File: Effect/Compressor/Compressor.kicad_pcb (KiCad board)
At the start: 2 copper layers, 30 x 62 mm, 33 parts, among them J1 Conn_01x04_Pin, J2 Conn_01x04_Pin, Q1 MMBF5103, Q2 NMB2227A, Q3 MMBF5103

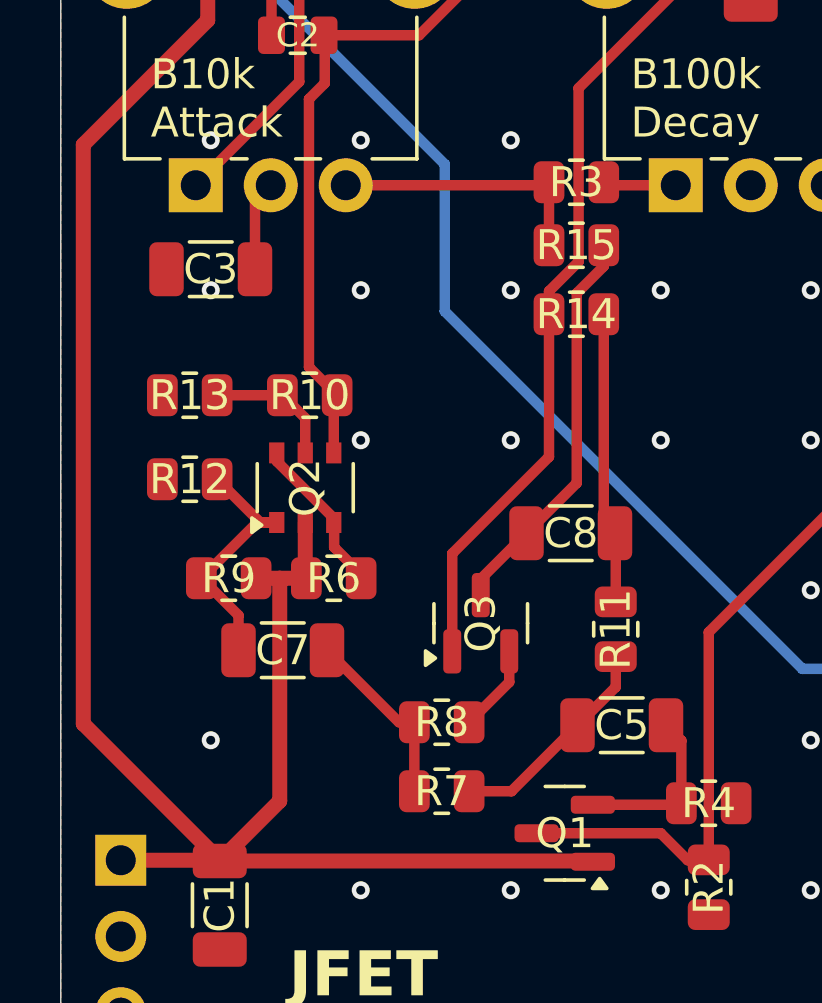
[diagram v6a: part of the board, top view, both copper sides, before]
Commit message: Update some compressor component values based on testing
I think I was being a bit too timid wrt the compressor, making it a bit
boring.  It definitely works, but it looks more interesting with a much
more aggressive compression ratio, and a more aggressive signal
amplification to match.

The level trim pot was also slow to respond because the capacitor to
keep it stable was fairly large.

Also, partially bypass the emitter resistor in the amplification stage
to give higher frequencies a bit more oomph - the AC signal analysis
claims they otherwise attenuated over 10kHz.

Most of this was tested with the old boards (just changed components).
And other parts are "this looks better in simulation" (eg the emitter
resistor bypassing).

Signed-off-by: Linus Torvalds <torvalds@linux-foundation.org>
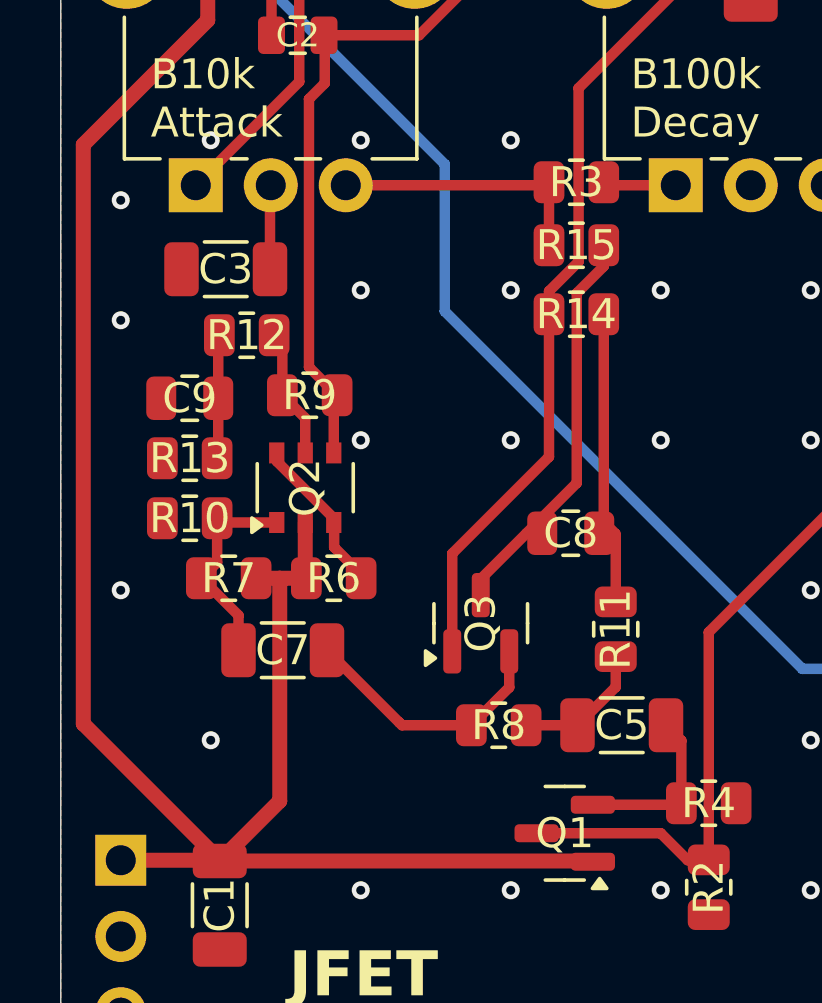
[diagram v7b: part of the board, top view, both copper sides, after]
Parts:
- removed the R8 at (97.7, 109.4)
- added C9: 22nF, Capacitor_SMD:C_0805_2012Metric, F.Cu at (89.3, 98.6)
- added R12: 470, Resistor_SMD:R_0805_2012Metric, F.Cu at (91.2, 96.5)
- C3: value 0.47uF -> 1uF
- C4: value 22uF -> 10uF
- C8: footprint Capacitor_SMD:C_1206_3216Metric -> Capacitor_SMD:C_0805_2012Metric
- R13: value 1k -> 470
- R8: renamed from R7; value 1k -> 470
- R9: renamed from R10; value 2k2 -> 10k
- moved R8 2.91 mm to (99.6, 109.5)
- moved R13 2.10 mm to (89.3, 100.6)
- moved R10 1.30 mm to (89.3, 102.6)
- moved C3 0.50 mm to (90.5, 94.3)
- renumbered R12 to R10, R9 to R7
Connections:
- Q3 pad 2: Net-(Q3-S) -> AMP_IN
- R13 pad 1: Net-(Q2A-E1) -> Net-(C9-Pad2)
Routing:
- net Net-(C9-Pad2): track 0.00 -> 4.13 mm
- net Net-(Q3-S): track 2.92 -> 0.00 mm
- net Net-(C5-Pad2): track 7.34 -> 4.53 mm
- net AMP_IN: track 6.21 -> 8.83 mm
- net Net-(Q2A-B1): track 8.78 -> 7.18 mm
- net Net-(Q3-G): track 14.1 -> 13.4 mm
- net GND: vias 39 -> 41

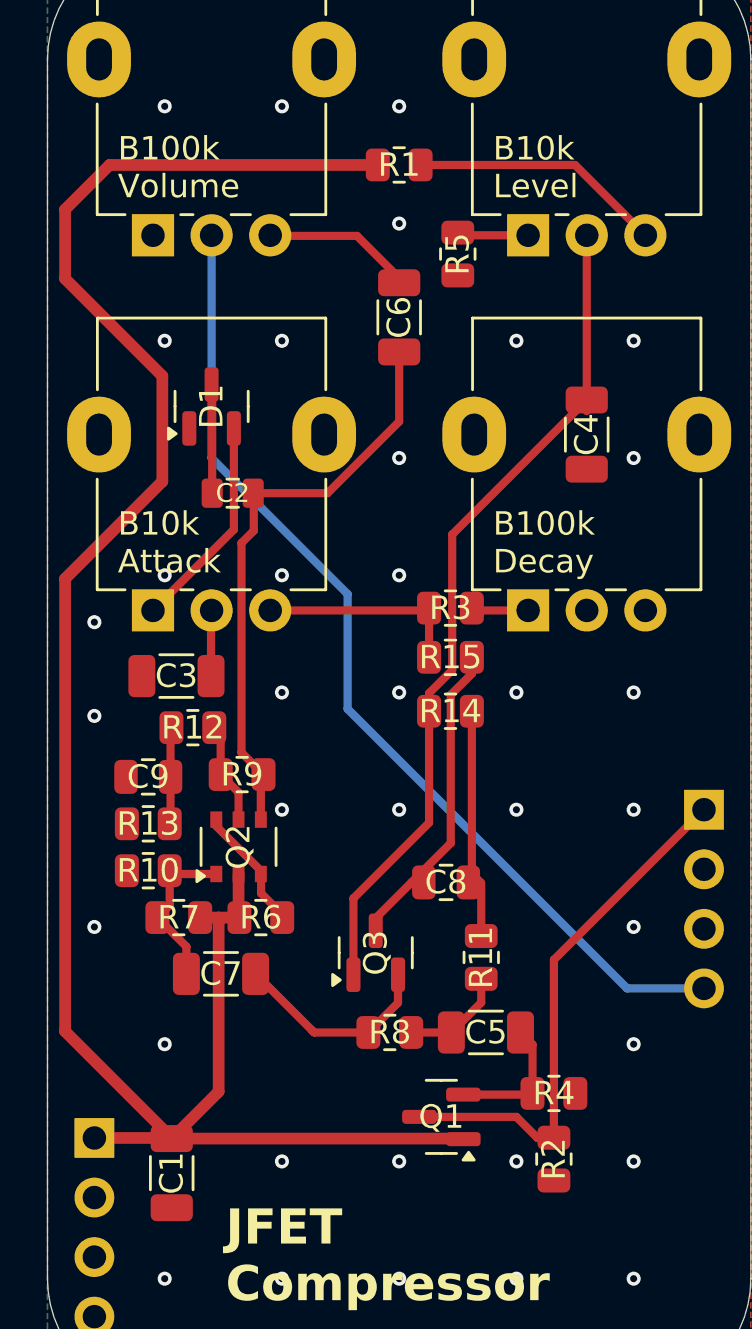
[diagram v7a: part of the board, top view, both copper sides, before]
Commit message: Compressor: More kicad file noise
This just re-annotates the schematic and undoes the workaround for the
kicad bug with crossed wires that has now been fixed.

Link: https://gitlab.com/kicad/code/kicad/-/issues/21480
Signed-off-by: Linus Torvalds <torvalds@linux-foundation.org>
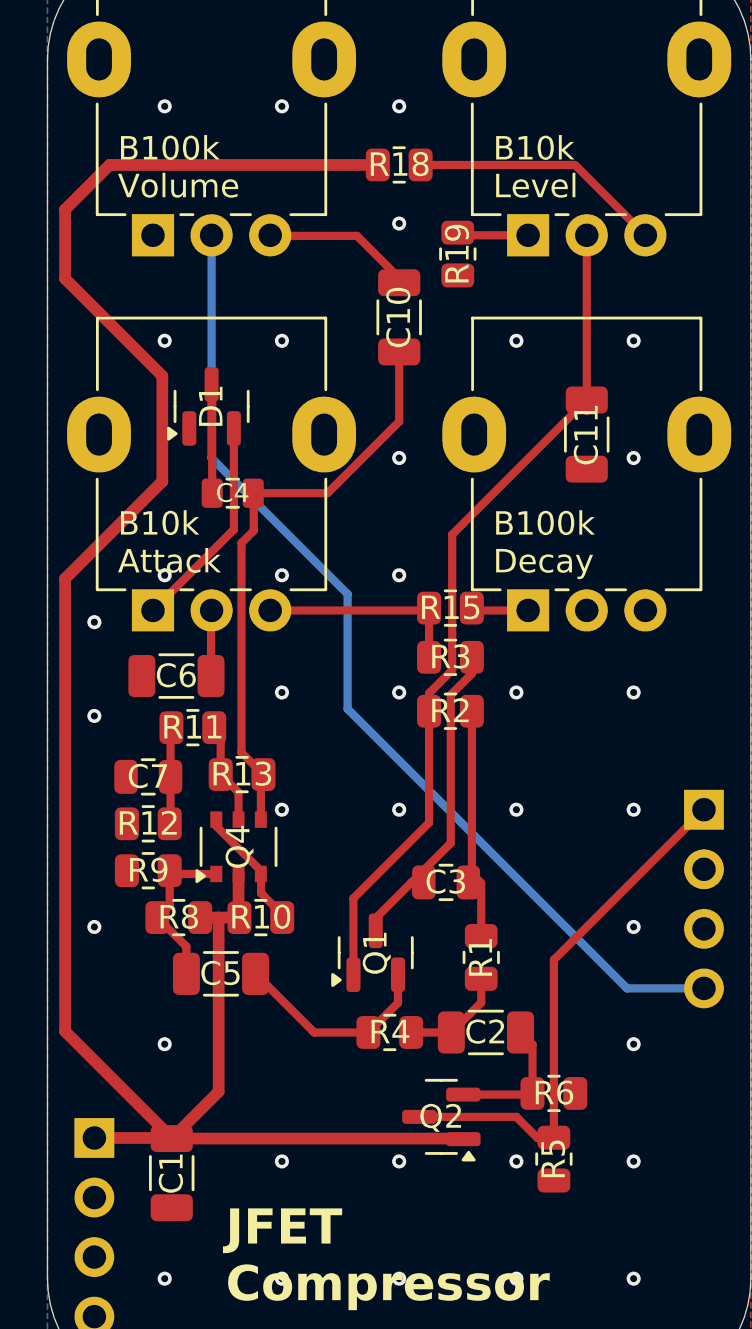
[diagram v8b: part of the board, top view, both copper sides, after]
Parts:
- renumbered C6 to C10, C4 to C11, C5 to C2, C8 to C3, C2 to C4, C7 to C5, C3 to C6, C9 to C7, Q3 to Q1, Q1 to Q2, Q2 to Q4, R11 to R1, R6 to R10, R12 to R11, R13 to R12, R9 to R13, R3 to R15, R1 to R18, R5 to R19, R14 to R2, R15 to R3, R8 to R4, R2 to R5, R4 to R6, R7 to R8, R10 to R9, RV3 to RV2, RV2 to RV3
